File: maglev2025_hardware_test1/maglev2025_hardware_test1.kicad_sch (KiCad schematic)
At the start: 106 parts, among them J1 SWD, J2 PWRIn, U1 RY8411, U10 INA240A1PW, U11 INA240A1PW, U12 INA240A1PW, U2 TMAG5170-Q1, U3 STM32G474RBTx, U4 RS3236, U5 AT8236, U6 AT8236, U7 AT8236, U8 AT8236, U9 INA240A1PW, Y1 25MHz

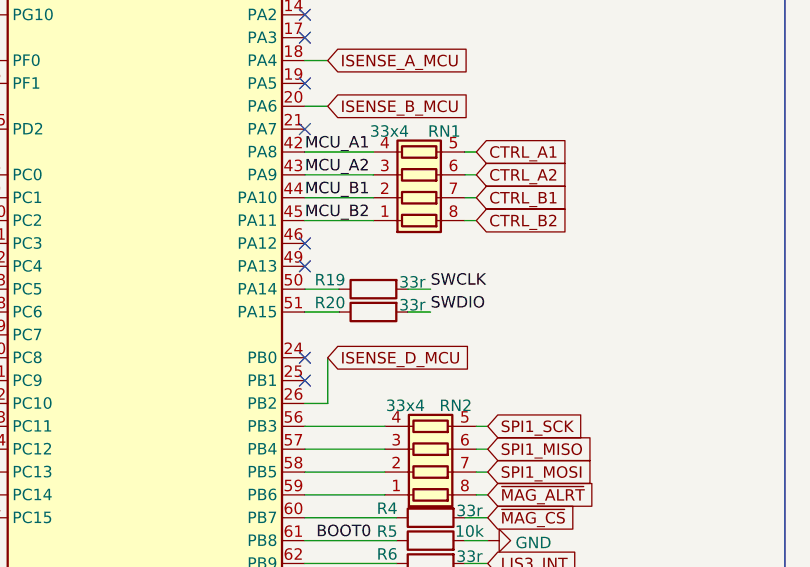
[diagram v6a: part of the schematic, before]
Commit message: Update PCB for soldering; Fix schematic bug (SWD Pin)
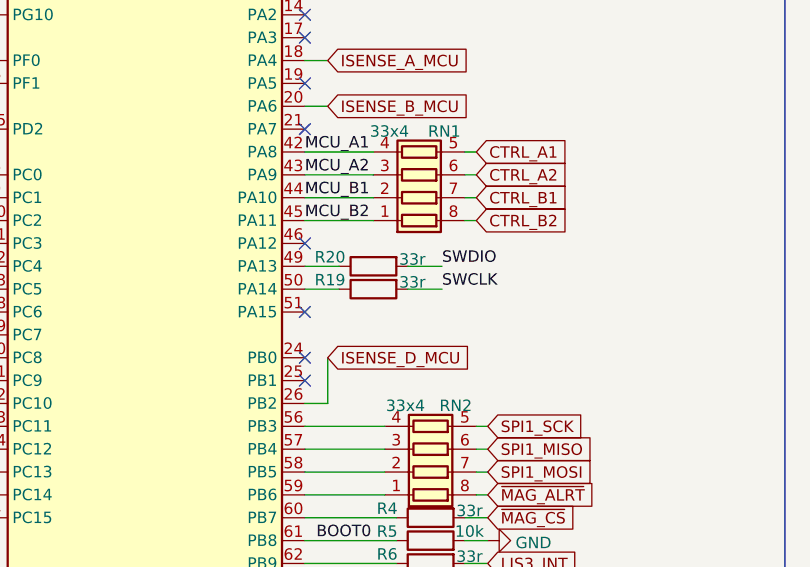
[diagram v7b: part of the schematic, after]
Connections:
- net at U3.49 (PA13): now also R20.1
- net at U3.51 (PA15): no longer R20.1
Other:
- moved on the sheet: R20
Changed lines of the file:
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@@
 	)
 	(no_connect
+		(at 87.63 76.2)
+	)
+	(no_connect
 		(at 87.63 50.8)
 	)
@@
 	)
 	(no_connect
-		(at 87.63 71.12)
-	)
-	(no_connect
 		(at 87.63 40.64)
 	)
@@
 	(wire
 		(pts
-			(xy 87.63 76.2) (xy 91.44 76.2)
-		)
-		(stroke
-			(width 0)
-			(type default)
-		)
-	)
-	(wire
-		(pts
 			(xy 365.76 133.35) (xy 360.68 133.35)
 		)
@@
 	(wire
 		(pts
-			(xy 99.06 76.2) (xy 101.6 76.2)
+			(xy 99.06 71.12) (xy 102.87 71.12)
 		)
 		(stroke
@@
 	(wire
 		(pts
+			(xy 87.63 71.12) (xy 91.44 71.12)
+		)
+		(stroke
+			(width 0)
+			(type default)
+		)
+	)
+	(wire
+		(pts
 			(xy 369.57 26.67) (xy 360.68 26.67)
 		)
@@
 	(wire
 		(pts
-			(xy 101.6 73.66) (xy 99.06 73.66)
+			(xy 102.87 73.66) (xy 99.06 73.66)
 		)
 		(stroke
@@
 	)
 	(label "SWDIO"
-		(at 101.6 76.2 0)
+		(at 102.87 71.12 0)
 		(effects
 			(font
@@
 	)
 	(label "SWCLK"
-		(at 101.6 73.66 0)
+		(at 102.87 73.66 0)
 		(effects
 			(font
@@
 	(symbol
 		(lib_id "Device:R")
-		(at 95.25 76.2 90)
+		(at 95.25 71.12 90)
 		(mirror x)
 		(unit 1)
@@
 		(dnp no)
 		(property "Reference" "R20"
-			(at 90.424 75.184 90)
+			(at 90.424 70.104 90)
 			(effects
 				(font
@@
 		)
 		(property "Value" "33r"
-			(at 99.568 75.438 90)
+			(at 99.568 70.358 90)
 			(effects
 				(font
@@
 		)
 		(property "Footprint" "Resistor_SMD:R_0603_1608Metric"
-			(at 95.25 74.422 90)
+			(at 95.25 69.342 90)
 			(effects
 				(font
@@
 		)
 		(property "Datasheet" "~"
-			(at 95.25 76.2 0)
+			(at 95.25 71.12 0)
 			(effects
 				(font
@@
 		)
 		(property "Description" "Resistor"
-			(at 95.25 76.2 0)
+			(at 95.25 71.12 0)
 			(effects
 				(font
